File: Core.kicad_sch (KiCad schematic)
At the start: 18 parts, among them J5 Conn_ARM_JTAG_SWD_10, U1 IMX6UL, U8 X1000, Y2 24MHz, Y3 32.768kHz

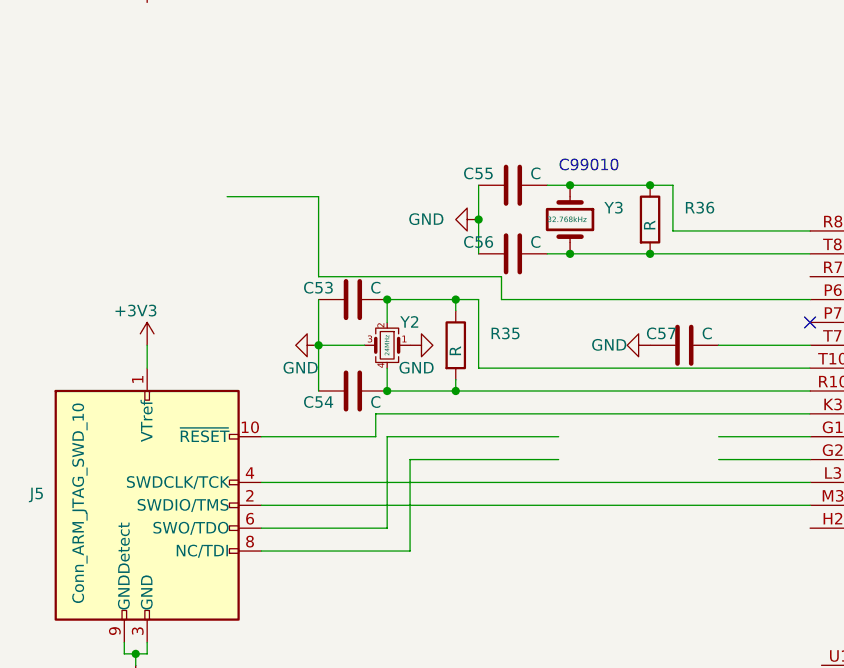
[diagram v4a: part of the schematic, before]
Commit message: update DDR
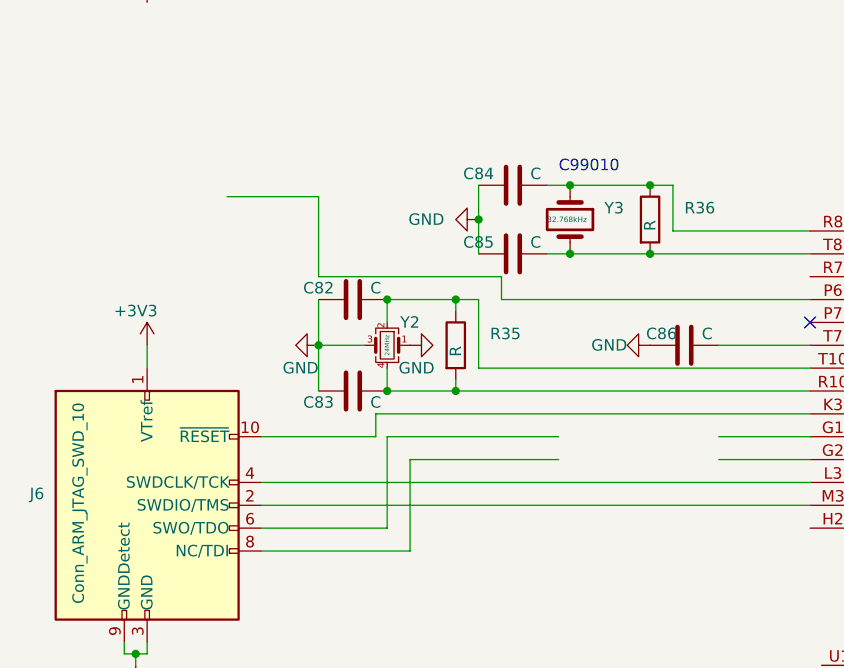
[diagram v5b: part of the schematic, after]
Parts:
- renumbered C53 to C82, C54 to C83, C55 to C84, C56 to C85, C57 to C86, J5 to J6
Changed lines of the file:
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@@
   (symbol (lib_id "power:GND") (at 35.56 100.33 0) (unit 1)
     (in_bom yes) (on_board yes) (fields_autoplaced)
-    (property "Reference" "#PWR074" (id 0) (at 35.56 106.68 0)
+    (property "Reference" "#PWR082" (id 0) (at 35.56 106.68 0)
       (effects (font (size 1.27 1.27)) hide)
     )
@@
   (symbol (lib_id "power:GND") (at 185.42 88.9 0) (unit 1)
     (in_bom yes) (on_board yes) (fields_autoplaced)
-    (property "Reference" "#PWR082" (id 0) (at 185.42 95.25 0)
+    (property "Reference" "#PWR090" (id 0) (at 185.42 95.25 0)
       (effects (font (size 1.27 1.27)) hide)
     )
@@
   (symbol (lib_id "Device:C") (at 77.47 46.99 90) (unit 1)
     (in_bom yes) (on_board yes)
-    (property "Reference" "C55" (id 0) (at 73.66 45.72 90))
+    (property "Reference" "C84" (id 0) (at 73.66 45.72 90))
     (property "Value" "C" (id 1) (at 80.01 45.72 90))
     (property "Footprint" "Capacitor_SMD:C_0402_1005Metric" (id 2) (at 81.28 46.0248 0)
@@
   (symbol (lib_id "power:+3V3") (at 190.5 67.31 0) (unit 1)
     (in_bom yes) (on_board yes)
-    (property "Reference" "#PWR083" (id 0) (at 190.5 71.12 0)
+    (property "Reference" "#PWR091" (id 0) (at 190.5 71.12 0)
       (effects (font (size 1.27 1.27)) hide)
     )
@@
   (symbol (lib_id "power:GND") (at 190.5 88.9 0) (unit 1)
     (in_bom yes) (on_board yes) (fields_autoplaced)
-    (property "Reference" "#PWR084" (id 0) (at 190.5 95.25 0)
+    (property "Reference" "#PWR092" (id 0) (at 190.5 95.25 0)
       (effects (font (size 1.27 1.27)) hide)
     )
@@
   (symbol (lib_id "Device:C") (at 96.52 64.77 90) (unit 1)
     (in_bom yes) (on_board yes)
-    (property "Reference" "C57" (id 0) (at 93.98 63.5 90))
+    (property "Reference" "C86" (id 0) (at 93.98 63.5 90))
     (property "Value" "C" (id 1) (at 99.06 63.5 90))
     (property "Footprint" "Capacitor_SMD:C_0402_1005Metric" (id 2) (at 100.33 63.8048 0)
@@
   (symbol (lib_id "Device:C") (at 77.47 54.61 90) (unit 1)
     (in_bom yes) (on_board yes)
-    (property "Reference" "C56" (id 0) (at 73.66 53.34 90))
+    (property "Reference" "C85" (id 0) (at 73.66 53.34 90))
     (property "Value" "C" (id 1) (at 80.01 53.34 90))
     (property "Footprint" "Capacitor_SMD:C_0402_1005Metric" (id 2) (at 81.28 53.6448 0)
@@
   (symbol (lib_id "power:GND") (at 55.88 64.77 270) (unit 1)
     (in_bom yes) (on_board yes)
-    (property "Reference" "#PWR077" (id 0) (at 49.53 64.77 0)
+    (property "Reference" "#PWR085" (id 0) (at 49.53 64.77 0)
       (effects (font (size 1.27 1.27)) hide)
     )
@@
   (symbol (lib_id "power:+3V3") (at 195.58 67.31 0) (unit 1)
     (in_bom yes) (on_board yes)
-    (property "Reference" "#PWR085" (id 0) (at 195.58 71.12 0)
+    (property "Reference" "#PWR093" (id 0) (at 195.58 71.12 0)
       (effects (font (size 1.27 1.27)) hide)
     )
@@
   (symbol (lib_id "power:+3V3") (at 36.83 64.77 0) (unit 1)
     (in_bom yes) (on_board yes)
-    (property "Reference" "#PWR076" (id 0) (at 36.83 68.58 0)
+    (property "Reference" "#PWR084" (id 0) (at 36.83 68.58 0)
       (effects (font (size 1.27 1.27)) hide)
     )
@@
   (symbol (lib_id "power:+3V3") (at 36.83 26.67 0) (unit 1)
     (in_bom yes) (on_board yes)
-    (property "Reference" "#PWR075" (id 0) (at 36.83 30.48 0)
+    (property "Reference" "#PWR083" (id 0) (at 36.83 30.48 0)
       (effects (font (size 1.27 1.27)) hide)
     )
@@
   (symbol (lib_id "power:GND") (at 92.71 64.77 270) (unit 1)
     (in_bom yes) (on_board yes)
-    (property "Reference" "#PWR080" (id 0) (at 86.36 64.77 0)
+    (property "Reference" "#PWR088" (id 0) (at 86.36 64.77 0)
       (effects (font (size 1.27 1.27)) hide)
     )
@@
   (symbol (lib_id "Connector:Conn_ARM_JTAG_SWD_10") (at 36.83 82.55 0) (unit 1)
     (in_bom yes) (on_board yes)
-    (property "Reference" "J5" (id 0) (at 25.4 81.2799 0)
+    (property "Reference" "J6" (id 0) (at 25.4 81.2799 0)
       (effects (font (size 1.27 1.27)) (justify right))
     )
@@
   (symbol (lib_id "Device:C") (at 59.69 59.69 90) (unit 1)
     (in_bom yes) (on_board yes)
-    (property "Reference" "C53" (id 0) (at 55.88 58.42 90))
+    (property "Reference" "C82" (id 0) (at 55.88 58.42 90))
     (property "Value" "C" (id 1) (at 62.23 58.42 90))
     (property "Footprint" "Capacitor_SMD:C_0402_1005Metric" (id 2) (at 63.5 58.7248 0)
@@
   (symbol (lib_id "power:GND") (at 73.66 50.8 270) (unit 1)
     (in_bom yes) (on_board yes)
-    (property "Reference" "#PWR079" (id 0) (at 67.31 50.8 0)
+    (property "Reference" "#PWR087" (id 0) (at 67.31 50.8 0)
       (effects (font (size 1.27 1.27)) hide)
     )
@@
   (symbol (lib_id "Device:C") (at 59.69 69.85 90) (unit 1)
     (in_bom yes) (on_board yes)
-    (property "Reference" "C54" (id 0) (at 55.88 71.12 90))
+    (property "Reference" "C83" (id 0) (at 55.88 71.12 90))
     (property "Value" "C" (id 1) (at 62.23 71.12 90))
     (property "Footprint" "Capacitor_SMD:C_0402_1005Metric" (id 2) (at 63.5 68.8848 0)
@@
   (symbol (lib_id "power:GND") (at 66.04 64.77 90) (unit 1)
     (in_bom yes) (on_board yes)
-    (property "Reference" "#PWR078" (id 0) (at 72.39 64.77 0)
+    (property "Reference" "#PWR086" (id 0) (at 72.39 64.77 0)
       (effects (font (size 1.27 1.27)) hide)
     )
@@
   (symbol (lib_id "power:+3V3") (at 185.42 67.31 0) (unit 1)
     (in_bom yes) (on_board yes)
-    (property "Reference" "#PWR081" (id 0) (at 185.42 71.12 0)
+    (property "Reference" "#PWR089" (id 0) (at 185.42 71.12 0)
       (effects (font (size 1.27 1.27)) hide)
     )
@@
   (symbol (lib_id "power:GND") (at 195.58 88.9 0) (unit 1)
     (in_bom yes) (on_board yes) (fields_autoplaced)
-    (property "Reference" "#PWR086" (id 0) (at 195.58 95.25 0)
-      (effects (font (size 1.27 1.27)) hide)
-    )
+    (property "Reference" "#PWR094" (id 0) (at 195.58 95.25 0)
+      (effects (font (size 1.27 1.27)) hide)
+    )
